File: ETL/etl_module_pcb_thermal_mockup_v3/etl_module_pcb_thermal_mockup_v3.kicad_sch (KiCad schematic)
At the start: 39 parts, among them J3 Conn_02x05_Counter_Clockwise, U1 ETROC_dummy_thermal_sensors, U2 ETROC_dummy_thermal_sensors, U3 ETROC_dummy_thermal_sensors, U4 ETROC_dummy_thermal_sensors, U5 AD77x8, U6 AD780, Y1 32kHz

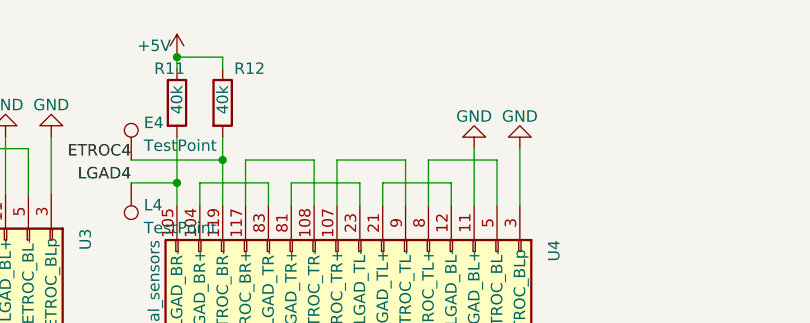
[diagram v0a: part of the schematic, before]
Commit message: Adds firmware and wirebonding instructions to ETL thermal mockup
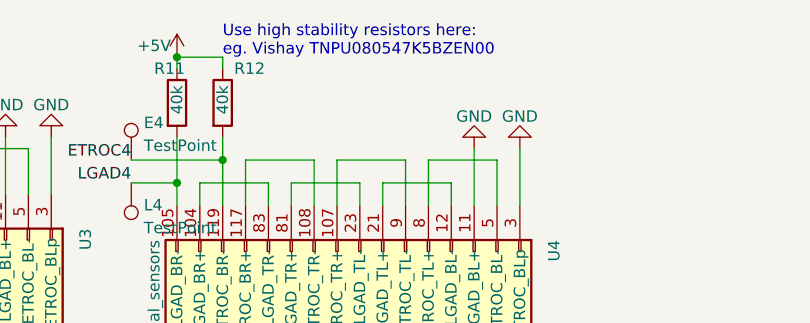
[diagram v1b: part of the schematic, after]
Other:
- note added: "Use high stability resistors here: eg. Vishay TNPU080547K5BZEN00"

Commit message: minor updates to pcb thermal mockup
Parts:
- R10, R11, R12, R5, R6, R7, R8, R9: value 40k -> 1k
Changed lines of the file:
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@@
       (effects (font (size 1.27 1.27)) (justify left))
     )
-    (property "Value" "40k" (at 144.78 31.75 90)
+    (property "Value" "1k" (at 144.78 31.75 90)
       (effects (font (size 1.27 1.27)) (justify left))
     )
@@
       (effects (font (size 1.27 1.27)) hide)
     )
-    (property "Datasheet" "~" (at 144.78 30.48 0)
+    (property "Datasheet" "https://www.digikey.com/en/products/detail/vishay-dale/TNPU08051K00AWEN00/11618132" (at 144.78 30.48 0)
       (effects (font (size 1.27 1.27)) hide)
     )
@@
       (effects (font (size 1.27 1.27)) (justify left))
     )
-    (property "Value" "40k" (at 92.71 31.75 90)
+    (property "Value" "1k" (at 92.71 31.75 90)
       (effects (font (size 1.27 1.27)) (justify left))
     )
@@
       (effects (font (size 1.27 1.27)) hide)
     )
-    (property "Datasheet" "~" (at 92.71 30.48 0)
+    (property "Datasheet" "https://www.digikey.com/en/products/detail/vishay-dale/TNPU08051K00AWEN00/11618132" (at 92.71 30.48 0)
       (effects (font (size 1.27 1.27)) hide)
     )
@@
       (effects (font (size 1.27 1.27)) (justify left))
     )
-    (property "Value" "40k" (at 97.79 31.75 90)
+    (property "Value" "1k" (at 97.79 31.75 90)
       (effects (font (size 1.27 1.27)) (justify left))
     )
@@
       (effects (font (size 1.27 1.27)) hide)
     )
-    (property "Datasheet" "~" (at 97.79 30.48 0)
+    (property "Datasheet" "https://www.digikey.com/en/products/detail/vishay-dale/TNPU08051K00AWEN00/11618132" (at 97.79 30.48 0)
       (effects (font (size 1.27 1.27)) hide)
     )
@@
       (effects (font (size 1.27 1.27)) (justify left))
     )
-    (property "Value" "40k" (at 40.64 31.75 90)
+    (property "Value" "1k" (at 40.64 31.75 90)
       (effects (font (size 1.27 1.27)) (justify left))
     )
@@
       (effects (font (size 1.27 1.27)) hide)
     )
-    (property "Datasheet" "~" (at 40.64 30.48 0)
+    (property "Datasheet" "https://www.digikey.com/en/products/detail/vishay-dale/TNPU08051K00AWEN00/11618132" (at 40.64 30.48 0)
       (effects (font (size 1.27 1.27)) hide)
     )
@@
       (effects (font (size 1.27 1.27)) (justify left))
     )
-    (property "Value" "40k" (at 201.93 33.02 90)
+    (property "Value" "1k" (at 201.93 33.02 90)
       (effects (font (size 1.27 1.27)) (justify left))
     )
@@
       (effects (font (size 1.27 1.27)) hide)
     )
-    (property "Datasheet" "~" (at 201.93 31.75 0)
+    (property "Datasheet" "https://www.digikey.com/en/products/detail/vishay-dale/TNPU08051K00AWEN00/11618132" (at 201.93 31.75 0)
       (effects (font (size 1.27 1.27)) hide)
     )
@@
       (effects (font (size 1.27 1.27)) (justify left))
     )
-    (property "Value" "40k" (at 45.72 31.75 90)
+    (property "Value" "1k" (at 45.72 31.75 90)
       (effects (font (size 1.27 1.27)) (justify left))
     )
@@
       (effects (font (size 1.27 1.27)) hide)
     )
-    (property "Datasheet" "~" (at 45.72 30.48 0)
+    (property "Datasheet" "https://www.digikey.com/en/products/detail/vishay-dale/TNPU08051K00AWEN00/11618132" (at 45.72 30.48 0)
       (effects (font (size 1.27 1.27)) hide)
     )
@@
       (effects (font (size 1.27 1.27)) (justify left))
     )
-    (property "Value" "40k" (at 196.85 33.02 90)
+    (property "Value" "1k" (at 196.85 33.02 90)
       (effects (font (size 1.27 1.27)) (justify left))
     )
@@
       (effects (font (size 1.27 1.27)) hide)
     )
-    (property "Datasheet" "~" (at 196.85 31.75 0)
+    (property "Datasheet" "https://www.digikey.com/en/products/detail/vishay-dale/TNPU08051K00AWEN00/11618132" (at 196.85 31.75 0)
       (effects (font (size 1.27 1.27)) hide)
     )
@@
       (effects (font (size 1.27 1.27)) (justify left))
     )
-    (property "Value" "40k" (at 149.86 31.75 90)
+    (property "Value" "1k" (at 149.86 31.75 90)
       (effects (font (size 1.27 1.27)) (justify left))
     )
@@
       (effects (font (size 1.27 1.27)) hide)
     )
-    (property "Datasheet" "~" (at 149.86 30.48 0)
-      (effects (font (size 1.27 1.27)) hide)
-    )
+    (property "Datasheet" "https://www.digikey.com/en/products/detail/vishay-dale/TNPU08051K00AWEN00/11618132" (at 149.86 30.48 0)
+      (effects (font (size 1.27 1.27)) hide)
+    )
